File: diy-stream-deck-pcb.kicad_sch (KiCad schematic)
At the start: 40 parts, among them J1 USB_C_Receptacle_USB2.0_16P, SW1 SW_Push, SW2 SW_Push, SW3 SW_Push, SW4 SW_Push, SW5 SW_Push, SW6 SW_Push, U1 USBLC6-2SC6, U2 AP2112K-3.3, U3 ESP32-C3-WROOM-02

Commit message: Fix: ERC inspection errors
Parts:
- R10, R11, R12, R13, R14, R15, R16, R17: footprint R_Axial_DIN0204_L3.6mm_D1.6mm_P1.90mm_Vertical -> Resistor_THT:R_Axial_DIN0207_L6.3mm_D2.5mm_P10.16mm_Horizontal
- renumbered C9 to C10, C5 to C6, C6 to C7, C7 to C8, C8 to C9
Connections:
- net GND: now also C1.2, C2.2

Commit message: Feat: add usb c model. Initial placement
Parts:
- SW3: value SW_Push -> CMD1; footprint Button_Switch_SMD:SW_Push_1P1T_NO_CK_KSC6xxJ -> Button_Switch_SMD:SW_SPST_B3U-1000P
- SW4: value SW_Push -> CMD2; footprint Button_Switch_SMD:SW_Push_1P1T_NO_CK_KSC6xxJ -> Button_Switch_SMD:SW_SPST_B3U-1000P
- SW5: value SW_Push -> CMD3; footprint Button_Switch_SMD:SW_Push_1P1T_NO_CK_KSC6xxJ -> Button_Switch_SMD:SW_SPST_B3U-1000P
- SW6: value SW_Push -> CMD4; footprint Button_Switch_SMD:SW_Push_1P1T_NO_CK_KSC6xxJ -> Button_Switch_SMD:SW_SPST_B3U-1000P
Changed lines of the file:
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@@
 			)
 		)
-		(property "Value" "SW_Push"
+		(property "Value" "CMD2"
 			(at 44.45 109.22 0)
 			(show_name no)
@@
 			)
 		)
-		(property "Footprint" "Button_Switch_SMD:SW_Push_1P1T_NO_CK_KSC6xxJ"
+		(property "Footprint" "Button_Switch_SMD:SW_SPST_B3U-1000P"
 			(at 44.45 109.22 0)
 			(hide yes)
@@
 			)
 		)
-		(property "Value" "SW_Push"
+		(property "Value" "CMD3"
 			(at 44.45 118.11 0)
 			(show_name no)
@@
 			)
 		)
-		(property "Footprint" "Button_Switch_SMD:SW_Push_1P1T_NO_CK_KSC6xxJ"
+		(property "Footprint" "Button_Switch_SMD:SW_SPST_B3U-1000P"
 			(at 44.45 118.11 0)
 			(hide yes)
@@
 			)
 		)
-		(property "Value" "SW_Push"
+		(property "Value" "CMD1"
 			(at 44.45 100.33 0)
 			(show_name no)
@@
 			)
 		)
-		(property "Footprint" "Button_Switch_SMD:SW_Push_1P1T_NO_CK_KSC6xxJ"
+		(property "Footprint" "Button_Switch_SMD:SW_SPST_B3U-1000P"
 			(at 44.45 100.33 0)
 			(hide yes)
@@
 			)
 		)
-		(property "Value" "SW_Push"
+		(property "Value" "CMD4"
 			(at 44.45 127 0)
 			(show_name no)
@@
 			)
 		)
-		(property "Footprint" "Button_Switch_SMD:SW_Push_1P1T_NO_CK_KSC6xxJ"
+		(property "Footprint" "Button_Switch_SMD:SW_SPST_B3U-1000P"
 			(at 44.45 127 0)
 			(hide yes)

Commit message: Feat: initial pcb layout
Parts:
- added J2: Conn_01x06_Pin, Connector_PinHeader_2.54mm:PinHeader_1x06_P2.54mm_Vertical, symbol Connector:Conn_01x06_Pin
- SW1: value SW_Push -> BOOT
- SW2: value SW_Push -> RESET
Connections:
- net +3V3: now also R17.1
- net IO1: now also J2.6 (Pin_6)
- net IO10: now also J2.3 (Pin_3)
- net IO2: now also J2.5 (Pin_5)
- net IO3: now also J2.4 (Pin_4)
- net IO7: no longer R17.1
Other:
- note added: "PINOUT"

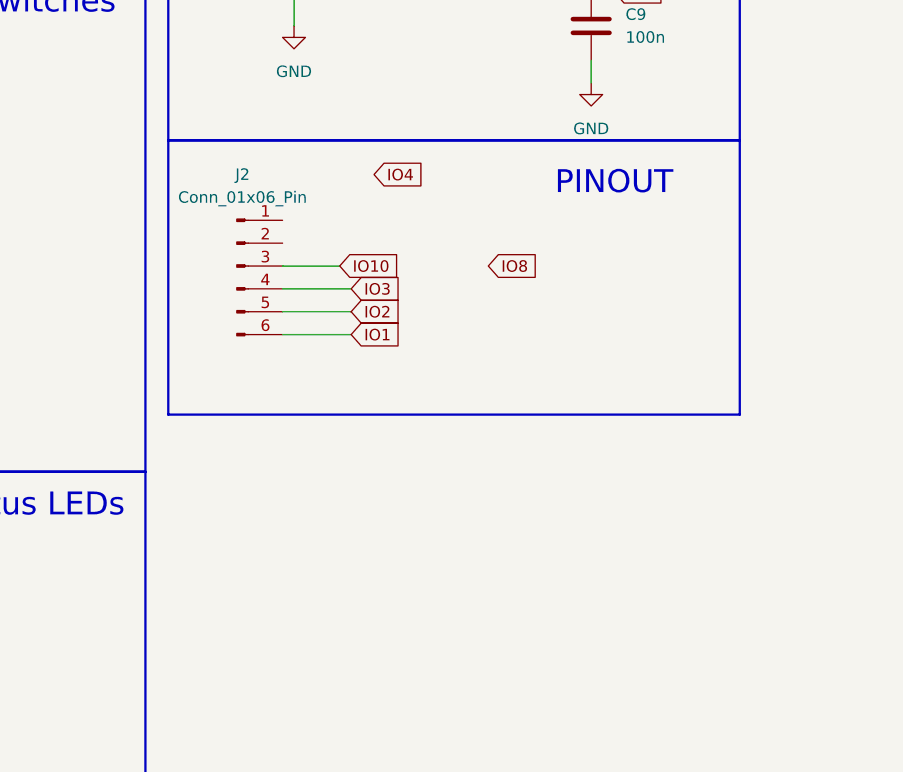
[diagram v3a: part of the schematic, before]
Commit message: Fix: usb footprint for 0.2mm copper-hole tolerance. DRC layout errors
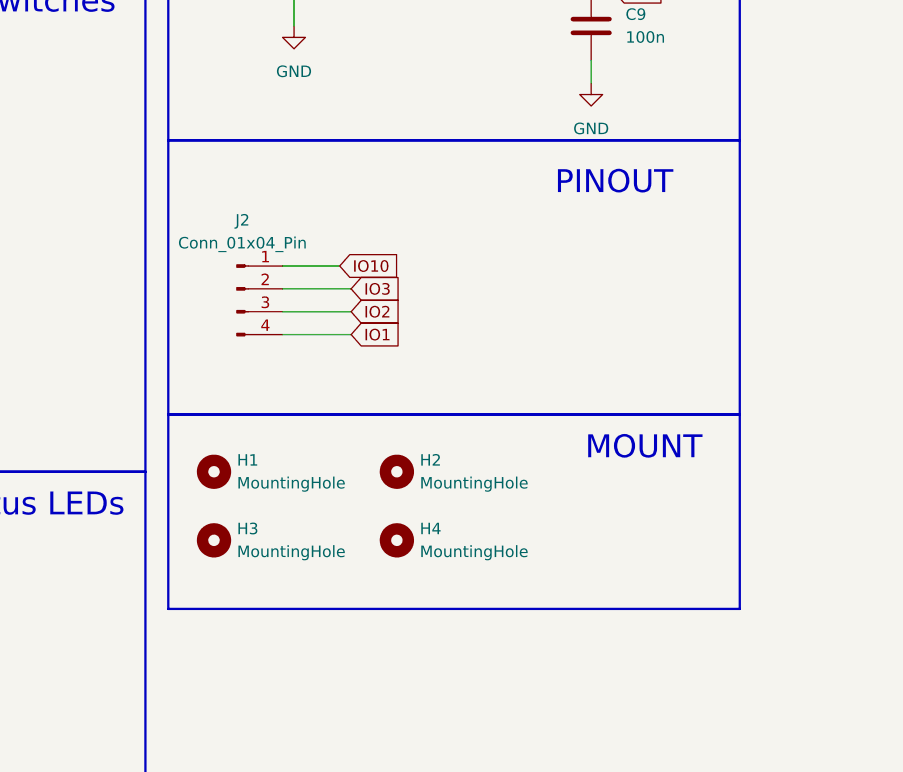
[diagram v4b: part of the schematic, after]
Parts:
- removed J2: Conn_01x06_Pin, Connector_PinHeader_2.54mm:PinHeader_1x06_P2.54mm_Vertical, symbol Connector:Conn_01x06_Pin
- added H1, H2, H3, H4: MountingHole, MountingHole:MountingHole_2.2mm_M2, symbol Mechanical:MountingHole
- added J2: Conn_01x04_Pin, Connector_PinHeader_2.54mm:PinHeader_1x04_P2.54mm_Vertical, symbol Connector:Conn_01x04_Pin
- J1: footprint Connector_USB:USB_C_Receptacle_G-Switch_GT-USB-7010ASV -> Connector_USB:USB_C_Receptacle_G-Switch_GT-USB-7025
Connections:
- net IO1: now also J2.4 (Pin_4)
- net IO10: now also J2.1 (Pin_1)
- net IO2: now also J2.3 (Pin_3)
- net IO3: now also J2.2 (Pin_2)
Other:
- note added: "MOUNT"

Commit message: Fix useless components
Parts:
- removed R3: 0, Resistor_SMD:R_0805_2012Metric, symbol Device:R
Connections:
- net VBUS is gone; now on net +5V: C1.1, D1.1 (K), J1.A4 (VBUS), J1.A9 (VBUS), J1.B4 (VBUS), J1.B9 (VBUS)
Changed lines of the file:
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@@
 	)
 	(junction
-		(at 224.79 20.32)
-		(diameter 0)
-		(color 0 0 0 0)
-	)
-	(junction
 		(at 176.53 24.13)
 		(diameter 0)
@@
 	(wire
 		(pts
-			(xy 245.11 20.32) (xy 247.65 20.32)
+			(xy 245.11 20.32) (xy 257.81 20.32)
 		)
 		(stroke
@@
 	(wire
 		(pts
-			(xy 217.17 20.32) (xy 224.79 20.32)
+			(xy 217.17 20.32) (xy 245.11 20.32)
 		)
 		(stroke
@@
 	(wire
 		(pts
-			(xy 255.27 20.32) (xy 257.81 20.32)
-		)
-		(stroke
-			(width 0)
-			(type default)
-		)
-	)
-	(wire
-		(pts
 			(xy 62.23 160.02) (xy 62.23 170.18)
 		)
@@
 	(wire
 		(pts
-			(xy 224.79 20.32) (xy 245.11 20.32)
-		)
-		(stroke
-			(width 0)
-			(type default)
-		)
-	)
-	(wire
-		(pts
 			(xy 217.17 33.02) (xy 232.41 33.02)
 		)
@@
 	)
 	(symbol
-		(lib_id "Device:R")
-		(at 251.46 20.32 270)
-		(unit 1)
-		(body_style 1)
-		(exclude_from_sim no)
-		(in_bom yes)
-		(on_board yes)
-		(in_pos_files yes)
-		(dnp no)
-		(fields_autoplaced yes)
-		(property "Reference" "R3"
-			(at 251.46 13.97 90)
-			(show_name no)
-			(do_not_autoplace no)
-			(effects
-				(font
-					(size 1.27 1.27)
-				)
-			)
-		)
-		(property "Value" "0"
-			(at 251.46 16.51 90)
-			(show_name no)
-			(do_not_autoplace no)
-			(effects
-				(font
-					(size 1.27 1.27)
-				)
-			)
-		)
-		(property "Footprint" "Resistor_SMD:R_0805_2012Metric"
-			(at 251.46 18.542 90)
-			(hide yes)
-			(show_name no)
-			(do_not_autoplace no)
-			(effects
-				(font
-					(size 1.27 1.27)
-				)
-			)
-		)
-		(property "Datasheet" ""
-			(at 251.46 20.32 0)
-			(hide yes)
-			(show_name no)
-			(do_not_autoplace no)
-			(effects
-				(font
-					(size 1.27 1.27)
-				)
-			)
-		)
-		(property "Description" "Resistor"
-			(at 251.46 20.32 0)
-			(hide yes)
-			(show_name no)
-			(do_not_autoplace no)
-			(effects
-				(font
-					(size 1.27 1.27)
-				)
-			)
-		)
-		(pin "2"
-		)
-		(pin "1"
-		)
-		(instances
-			(project "diy-stream-deck-pcb"
-				(path "/6446e006-a6c3-4f5c-b769-2813a7a1b115"
-					(reference "R3")
-					(unit 1)
-				)
-			)
-		)
-	)
-	(symbol
 		(lib_id "RF_Module:ESP32-C3-WROOM-02")
 		(at 62.23 57.15 0)
@@
 					(unit 1)
 				)
-			)
-		)
-	)
-	(symbol
-		(lib_id "power:PWR_FLAG")
-		(at 224.79 20.32 0)
-		(unit 1)
-		(body_style 1)
-		(exclude_from_sim no)
-		(in_bom yes)
-		(on_board yes)
-		(in_pos_files yes)
-		(dnp no)
-		(fields_autoplaced yes)
-		(property "Reference" "#FLG01"
-			(at 224.79 18.415 0)
-			(hide yes)
-			(show_name no)
-			(do_not_autoplace no)
-			(effects
-				(font
-					(size 1.27 1.27)
-				)
-			)
-		)
-		(property "Value" "PWR_FLAG"
-			(at 224.79 15.24 0)
-			(show_name no)
-			(do_not_autoplace no)
-			(effects
-				(font
-					(size 1.27 1.27)
-				)
-			)
-		)
-		(property "Footprint" ""
-			(at 224.79 20.32 0)
-			(hide yes)
-			(show_name no)
-			(do_not_autoplace no)
-			(effects
-				(font
-					(size 1.27 1.27)
-				)
-			)
-		)
-		(property "Datasheet" ""
-			(at 224.79 20.32 0)
-			(hide yes)
-			(show_name no)
-			(do_not_autoplace no)
-			(effects
-				(font
-					(size 1.27 1.27)
-				)
-			)
-		)
-		(property "Description" "Special symbol for telling ERC where power comes from"
-			(at 224.79 20.32 0)
-			(hide yes)
-			(show_name no)
-			(do_not_autoplace no)
-			(effects
-				(font
-					(size 1.27 1.27)
-				)
-			)
-		)
-		(pin "1"
-		)
-		(instances
-			(project "diy-stream-deck-pcb"
-				(path "/6446e006-a6c3-4f5c-b769-2813a7a1b115"
-					(reference "#FLG01")
-					(unit 1)
-				)
